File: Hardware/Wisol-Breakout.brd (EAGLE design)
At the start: 21.6 x 25.4 mm, 13 parts

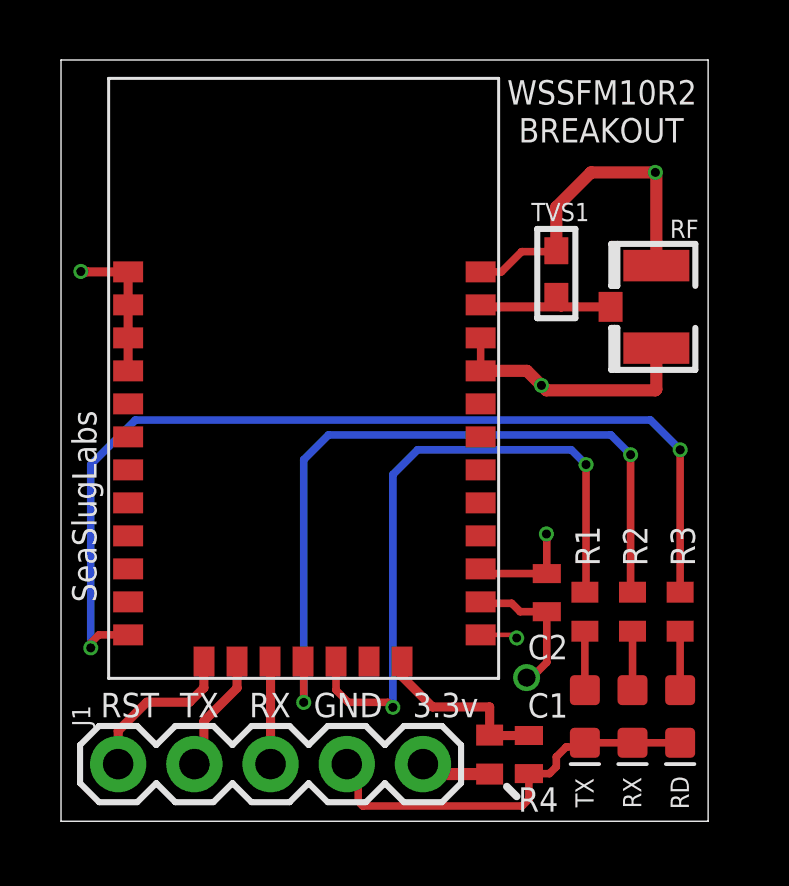
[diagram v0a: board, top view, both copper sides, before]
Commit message: Updated for Seeed PCB Assembly
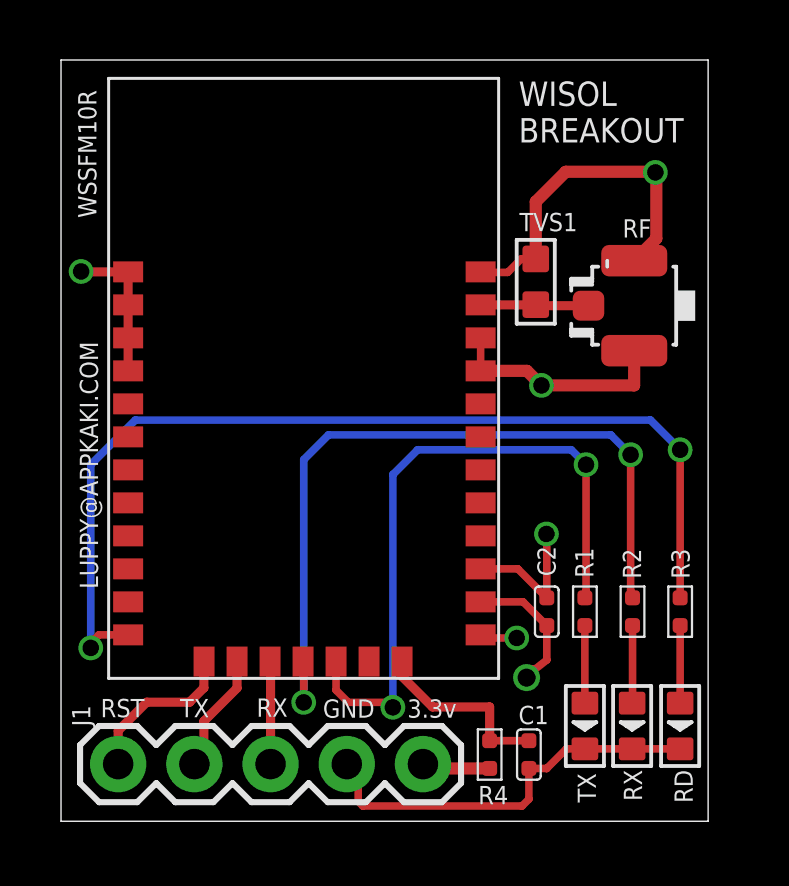
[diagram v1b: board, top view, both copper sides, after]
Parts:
- removed WSSFM10R2: WSSFM10R2/R4WSSFM10R2R4, SigfoxMod-RCZ1:WISOL
- added WSSFM10R: WSSFM10RWSSFM10R2R4, WisolWSSFM10R:WSSFM10R
- C1, C2: value 0.1uF -> 100nf; device IoTthings:0402 -> Seeed-Capacitor:C0402
- R1, R2, R3: value (none) -> 1K; device IoTthings:R0402 -> Seeed-Resistor:R0402
- R4: value 100k -> 100K 1/16W; device IoTthings:R0402 -> Seeed-Resistor:R0402
- RD, RX, TX: device IoTthings:LED-0603 -> Seeed-LED:LED-0603
- RF: value (none) -> U-FL; device IoTthings:U.FL -> Seeed-Connector:U-FL3P-SMD-2.6X2.6X1.0MM
- TVS1: value TVS-0603 -> 1K 1/10W; device supressor:TVS0603 -> Seeed-Fuse:D0603
- moved TVS1 0.74 mm to (48.5, 45.3), turned to 180 degrees
- moved RF 0.74 mm to (51.8, 44.5), turned to 0 degrees
- moved C2 0.63 mm to (48.9, 34.3), turned to 0 degrees
- moved RX 0.32 mm to (51.7, 30.5)
- moved RD 0.32 mm to (53.3, 30.5)
- moved TX 0.32 mm to (50.2, 30.5)
- turned C1 to 180 degrees
- turned R1 to 0 degrees
- turned R2 to 0 degrees
- turned R3 to 0 degrees
- turned R4 to 0 degrees
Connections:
- net 3.3V: now also WSSFM10R.21; no longer WSSFM10R2.21
- net GND: now also RD.-, RF.GND1, RF.GND2, RX.-, TX.-, WSSFM10R.1, WSSFM10R.2, WSSFM10R.20, WSSFM10R.22, WSSFM10R.28, WSSFM10R.29, WSSFM10R.3, WSSFM10R.31, WSSFM10R.4; no longer RD.C, RF.1, RF.2, RX.C, TX.C, WSSFM10R2.1, WSSFM10R2.2, WSSFM10R2.20, WSSFM10R2.22, WSSFM10R2.28, WSSFM10R2.29, WSSFM10R2.3, WSSFM10R2.31, WSSFM10R2.4
- net GPIO1: now also WSSFM10R.24; no longer WSSFM10R2.24
- net GPIO2: now also WSSFM10R.25; no longer WSSFM10R2.25
- net N$1: now also WSSFM10R.19; no longer WSSFM10R2.19
- net N$2: now also TX.+; no longer TX.A
- net N$3: now also RX.+; no longer RX.A
- net N$4: now also RD.+; no longer RD.A
- net RADIO_LED: now also WSSFM10R.12; no longer WSSFM10R2.12
- net RF_OUT: now also RF.D, WSSFM10R.30; no longer RF.3, WSSFM10R2.30
- net RST_N: now also WSSFM10R.13; no longer WSSFM10R2.13
- net RX_LED: now also WSSFM10R.16; no longer WSSFM10R2.16
- net TX_LED: now also WSSFM10R.17; no longer WSSFM10R2.17
- net WISOL_RX: now also WSSFM10R.15; no longer WSSFM10R2.15
- net WISOL_TX: now also WSSFM10R.14; no longer WSSFM10R2.14
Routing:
- net RF_OUT: track 4.82 -> 3.61 mm
- net N$3: track 1.97 -> 2.59 mm
- net N$4: track 1.97 -> 2.59 mm
- net N$2: track 1.97 -> 2.59 mm
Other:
- board text added: "LUPPY@APPKAKI.COM"
- board text added: "WISOL BREAKOUT"
- board text removed: "BREAKOUT"
- board text removed: "SeaSlugLabs"

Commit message: Added RF inductor as recommended by Wisol H/W Design Guide
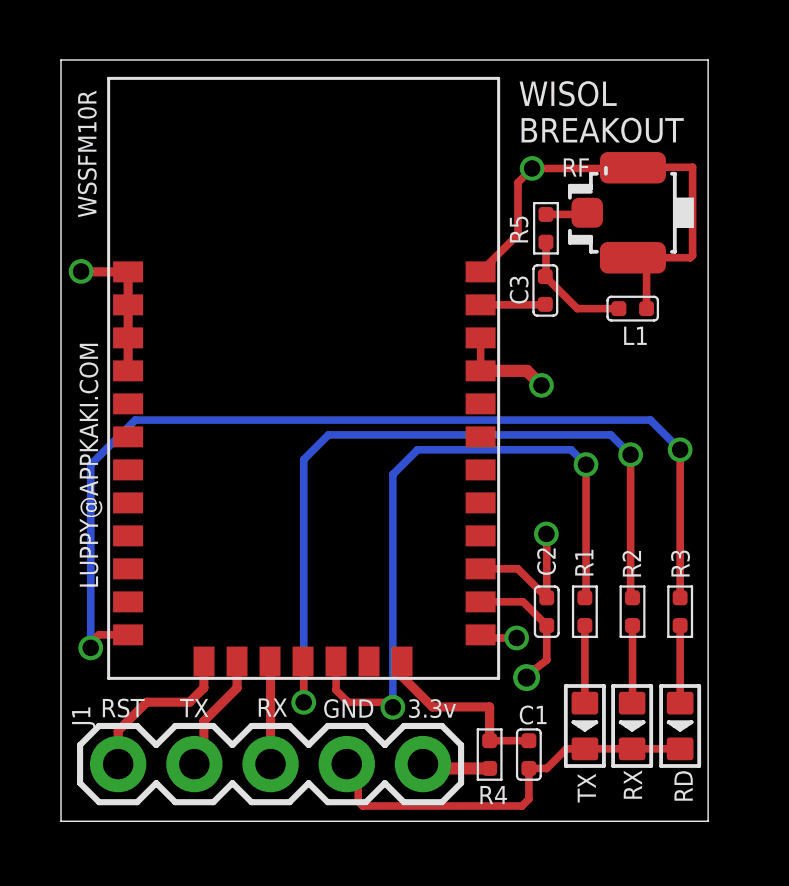
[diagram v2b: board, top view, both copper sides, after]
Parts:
- removed TVS1: 1K 1/10W, Seeed-Fuse:D0603
- added C3: 100pf, Seeed-Capacitor:C0402
- added L1: 47NH, Seeed-Inductor:L0402
- added R5: 0R, Seeed-Resistor:R0402
- moved RF 3.10 mm to (51.8, 47.6)
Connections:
- new net N$5: C3.2, L1.1, R5.1
- new net N$6: R5.2, RF.D
- net GND: now also L1.2; no longer TVS1.2
- net RF_OUT: now also C3.1; no longer RF.D, TVS1.1
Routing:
- net N$5: track 0.00 -> 4.07 mm
- net RF_OUT: track 3.61 -> 2.16 mm
- net N$6: track 0.00 -> 1.40 mm
- net GND: track 43.6 -> 44.1 mm

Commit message: Added revision
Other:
- board text added: "REV A"
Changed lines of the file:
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@@
 <drawing>
 <settings>
-<setting alwaysvectorfont="yes"/>
+<setting alwaysvectorfont="no"/>
 <setting keepoldvectorfont="yes"/>
 <setting verticaltext="up"/>
@@
 <dimension x1="32.7025" y1="27.305" x2="32.7025" y2="52.705" x3="27.305" y3="40.005" textsize="1.778" layer="51"/>
 <text x="33.937109375" y="35.05105" size="0.6096" layer="21" font="vector" ratio="16" rot="R90">LUPPY@APPKAKI.COM</text>
+<text x="53.227296875" y="42.147434375" size="0.6096" layer="21" font="vector" ratio="16" rot="R180">REV A</text>
 </plain>
 <attributes>
